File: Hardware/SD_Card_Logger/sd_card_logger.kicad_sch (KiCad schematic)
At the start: 4 parts, among them J1 MEM2090-00-145-00-A, U1 EMIF06-MSD02N16

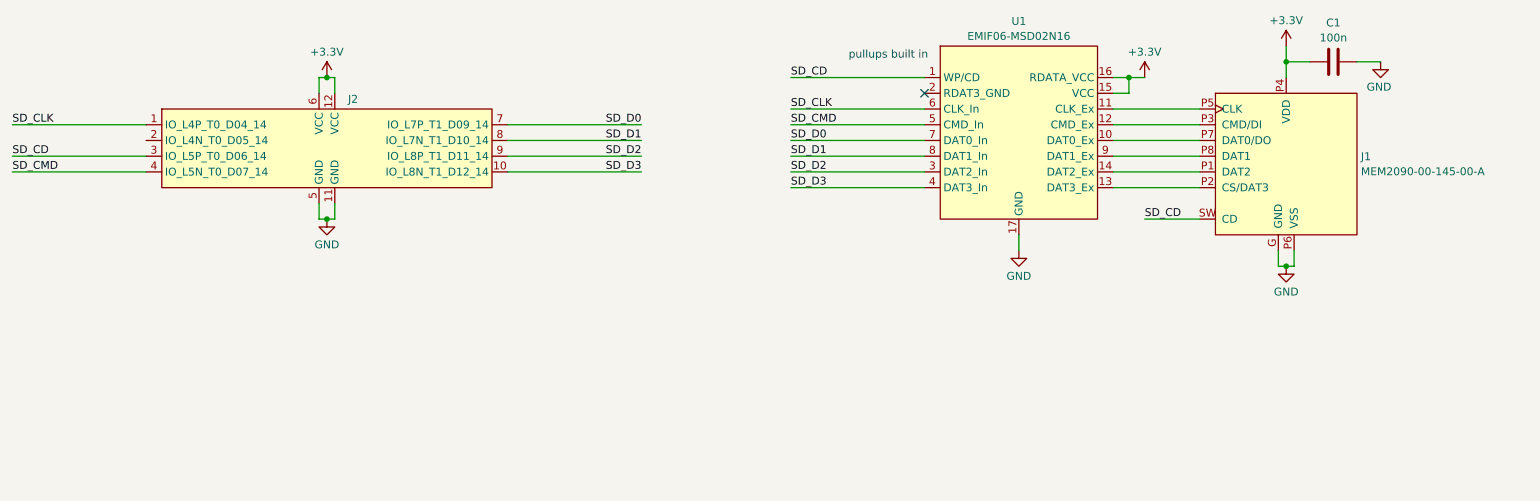
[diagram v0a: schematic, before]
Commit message: Finish SD card logger PCB and reorganize RTL a bit
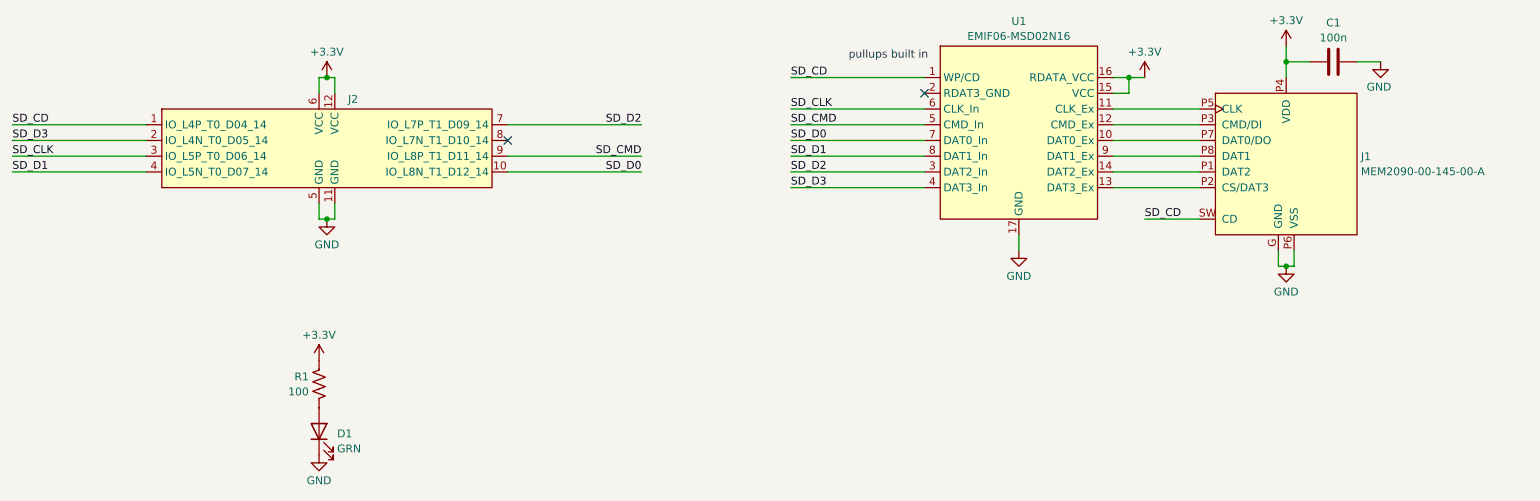
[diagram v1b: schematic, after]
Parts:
- added D1: GRN, LED_SMD:LED_0805_2012Metric, symbol Device:LED
- added R1: 100, Resistor_SMD:R_0805_2012Metric, symbol Device:R_US
- C1: footprint Capacitor_SMD:C_0603_1608Metric -> Capacitor_SMD:C_0805_2012Metric
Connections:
- net +3.3V: now also R1.1
- net GND: now also D1.1 (K)
- net SD_CD: now also J2.1 (IO_L4P_T0_D04_14); no longer J2.3 (IO_L5P_T0_D06_14)
- net SD_CLK: now also J2.3 (IO_L5P_T0_D06_14); no longer J2.1 (IO_L4P_T0_D04_14)
- net SD_CMD: now also J2.9 (IO_L8P_T1_D11_14); no longer J2.4 (IO_L5N_T0_D07_14)
- net SD_D0: now also J2.10 (IO_L8N_T1_D12_14); no longer J2.7 (IO_L7P_T1_D09_14)
- net SD_D1: now also J2.4 (IO_L5N_T0_D07_14); no longer J2.8 (IO_L7N_T1_D10_14)
- net SD_D2: now also J2.7 (IO_L7P_T1_D09_14); no longer J2.9 (IO_L8P_T1_D11_14)
- net SD_D3: now also J2.2 (IO_L4N_T0_D05_14); no longer J2.10 (IO_L8N_T1_D12_14)
- new net: D1.2 (A), R1.2
- no-connect marks 1 -> 2
